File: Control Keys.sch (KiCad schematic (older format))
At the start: 4 parts

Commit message: Fixed PISO Shift Register Wiring
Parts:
- added U?: SN74LVC1G04DBVR, digikey-footprints:SOT-753, symbol dk_Logic-Gates-and-Inverters:SN74LVC1G04DBVR
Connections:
- net GND: now also U?.3 (GND); no longer U?.13 (~SLoad), U?.13 (~SLoad)
- net SHIFT_RCLK: now also U?.2 (A)
- net VCC: now also U?.5 (VCC)
- new net: U?.13 (~SLoad), U?.13 (~SLoad), U?.4 (Y)
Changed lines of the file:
@@
 	4950 1600 4950 2100
-Wire Wire Line
-	4950 1600 6150 1600
 Wire Wire Line
 	6950 1600 6950 2100
@@
 	6250 2300 6400 2300
 Connection ~ 4250 1400
-Wire Wire Line
-	4400 2450 4150 2450
-Wire Wire Line
-	4150 2450 4150 1600
 Connection ~ 4150 1600
 Wire Wire Line
@@
 Connection ~ 4050 1500
 Wire Wire Line
-	6400 2450 6150 2450
-Wire Wire Line
-	6150 2450 6150 1600
-Connection ~ 6150 1600
-Wire Wire Line
-	6150 1600 6800 1600
-Wire Wire Line
 	4050 1500 6050 1500
 Wire Wire Line
@@
 	6050 2550 6050 1500
 Wire Wire Line
-	4150 2450 4150 2750
-Wire Wire Line
 	4150 2750 4400 2750
-Connection ~ 4150 2450
 $Comp
 L Device:C C?
@@
 	9350 1300 9350 3550
 Wire Wire Line
-	1300 1600 1300 4800
+	1300 1600 1300 2000
 Wire Wire Line
 	4650 4800 1300 4800
@@
 	7500 3550 9350 3550
 Wire Wire Line
-	1500 1100 5100 1100
+	1500 1100 2550 1100
 Connection ~ 1500 1100
 Wire Wire Line
@@
 	1000 1400 4250 1400
 Wire Wire Line
-	1000 1500 4050 1500
+	1000 1500 2000 1500
 Wire Wire Line
 	1300 1600 4150 1600
 Connection ~ 1300 1600
-Wire Bus Line
-	4200 2950 4200 4400
-Wire Bus Line
-	6100 2950 6100 4400
-Wire Bus Line
-	6250 4400 6250 6300
 $Sheet
 S 4650 4600 1250 1700
@@
 F3 "GND" I L 2700 5800 50
 $EndSheet
+$Comp
+L dk_Logic-Gates-and-Inverters:SN74LVC1G04DBVR U?
+U 1 1 5EE64350
+P 2000 2100
+AR Path="/5E8C755A/5EE64350" Ref="U?"  Part="1"
+AR Path="/5E8C79BD/5EE64350" Ref="U?"  Part="1"
+F 0 "U?" V 1897 2344 60  0000 L CNN
+F 1 "SN74LVC1G04DBVR" V 2003 2344 60  0000 L CNN
+F 2 "digikey-footprints:SOT-753" H 2200 2300 60  0001 L CNN
+F 3 "http://www.ti.com/general/docs/suppproductinfo.tsp?distId=10&gotoUrl=http%3A%2F%2Fwww.ti.com%2Flit%2Fgpn%2Fsn74lvc1g04" H 2200 2400 60  0001 L CNN
+F 4 "296-11599-1-ND" H 2200 2500 60  0001 L CNN "Digi-Key_PN"
+F 5 "SN74LVC1G04DBVR" H 2200 2600 60  0001 L CNN "MPN"
+F 6 "Integrated Circuits (ICs)" H 2200 2700 60  0001 L CNN "Category"
+F 7 "Logic - Gates and Inverters" H 2200 2800 60  0001 L CNN "Family"
+F 8 "http://www.ti.com/general/docs/suppproductinfo.tsp?distId=10&gotoUrl=http%3A%2F%2Fwww.ti.com%2Flit%2Fgpn%2Fsn74lvc1g04" H 2200 2900 60  0001 L CNN "DK_Datasheet_Link"
+F 9 "/product-detail/en/texas-instruments/SN74LVC1G04DBVR/296-11599-1-ND/385738" H 2200 3000 60  0001 L CNN "DK_Detail_Page"
+F 10 "IC INVERTER 1CH 1-INP SOT23-5" H 2200 3100 60  0001 L CNN "Description"
+F 11 "Texas Instruments" H 2200 3200 60  0001 L CNN "Manufacturer"
+F 12 "Active" H 2200 3300 60  0001 L CNN "Status"
+	1    2000 2100
+	0    1    1    0
+$EndComp
+Wire Wire Line
+	2000 1800 2000 1500
+Connection ~ 2000 1500
+Wire Wire Line
+	2000 1500 4050 1500
+Wire Wire Line
+	1800 2000 1300 2000
+Connection ~ 1300 2000
+Wire Wire Line
+	1300 2000 1300 4800
+Wire Wire Line
+	2200 2100 2550 2100
+Wire Wire Line
+	2550 2100 2550 1100
+Connection ~ 2550 1100
+Wire Wire Line
+	2550 1100 5100 1100
+Wire Wire Line
+	4150 1600 4150 2750
+Wire Wire Line
+	4950 1600 6800 1600
+Wire Wire Line
+	2000 2300 2000 2450
+Wire Wire Line
+	2000 2450 3300 2450
+Wire Wire Line
+	3300 2450 3300 1200
+Wire Wire Line
+	3300 1200 6150 1200
+Wire Wire Line
+	6150 1200 6150 2450
+Wire Wire Line
+	6150 2450 6400 2450
+Wire Bus Line
+	4200 2950 4200 4400
+Wire Bus Line
+	6100 2950 6100 4400
+Wire Bus Line
+	6250 4400 6250 6300
+Connection ~ 3300 2450
+Wire Wire Line
+	3300 2450 4400 2450
 $EndSCHEMATC

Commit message: Corrected errors found in design rule check
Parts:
- removed U? (x2): 74LS597, symbol 74xx_IEEE:74LS597
- added U10, U11: 74LS597, Package_SO:SOIC-16_3.9x9.9mm_P1.27mm, symbol 74xx_IEEE:74LS597
- C43, C44: renamed from C?; footprint (none) -> Capacitor_SMD:C_1206_3216Metric_Pad1.42x1.75mm_HandSolder
- gave numbers to parts that had none: 1
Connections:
- net DEL: now also U10.6 (G)
- net DN: now also U11.3 (D)
- net END: now also U10.7 (H)
- net EXT10: now also U11.7 (H)
- net EXT8: now also U11.5 (F)
- net EXT9: now also U11.6 (G)
- net GND: now also U10.14 (SER), U10.8 (GND), U11.8 (GND)
- net HOME: now also U10.4 (E)
- net INS: now also U10.3 (D)
- net LT: now also U11.2 (C)
- net PAUS: now also U10.2 (C)
- net PGDN: now also U11.15 (A)
- net PGUP: now also U10.5 (F)
- net PRNT: now also U10.15 (A)
- net RESET: now also U10.10 (~R), U11.10 (~R)
- net RT: now also U11.4 (E)
- net SCRL: now also U10.1 (B)
- net SHIFT_4_DATA: now also U11.9 (QH)
- net SHIFT_CLK: now also U10.11 (SCK), U11.11 (SCK)
- net SHIFT_RCLK: now also U10.12 (CLK), U11.12 (CLK)
- net UP: now also U11.1 (B)
- net VCC: now also U10.16 (VCC), U11.16 (VCC)
- net at U9.4 (Y): now also U10.13 (~SLoad), U11.13 (~SLoad)
- new net: U10.9 (QH), U11.14 (SER)
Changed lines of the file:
@@
 Text HLabel 10600 1300 2    50   Output ~ 0
 SHIFT_4_DATA
-$Comp
-L 74xx_IEEE:74LS597 U?
-U 1 1 6064AC4A
-P 4950 2900
-AR Path="/5E8C77AE/6064AC4A" Ref="U?"  Part="1"
-AR Path="/5E8C755A/6064AC4A" Ref="U?"  Part="1"
-AR Path="/5E8C79BD/6064AC4A" Ref="U?"  Part="1"
-F 0 "U?" H 4950 3916 50  0000 C CNN
-F 1 "74LS597" H 4950 3825 50  0000 C CNN
-F 2 "" H 4950 2900 50  0001 C CNN
-F 3 "" H 4950 2900 50  0001 C CNN
-	1    4950 2900
-	1    0    0    -1
-$EndComp
-$Comp
-L 74xx_IEEE:74LS597 U?
-U 1 1 6064AC50
-P 6950 2900
-AR Path="/5E8C77AE/6064AC50" Ref="U?"  Part="1"
-AR Path="/5E8C755A/6064AC50" Ref="U?"  Part="1"
-AR Path="/5E8C79BD/6064AC50" Ref="U?"  Part="1"
-F 0 "U?" H 6950 3916 50  0000 C CNN
-F 1 "74LS597" H 6950 3825 50  0000 C CNN
-F 2 "" H 6950 2900 50  0001 C CNN
-F 3 "" H 6950 2900 50  0001 C CNN
-	1    6950 2900
-	1    0    0    -1
-$EndComp
 Wire Wire Line
 	4250 1400 4250 2300
@@
 Wire Wire Line
 	5600 2750 6400 2750
-Wire Wire Line
-	5100 1100 5100 2100
 Wire Wire Line
 	4950 1600 4950 2100
@@
 Connection ~ 4950 1600
 Wire Wire Line
-	5100 1100 7100 1100
-Wire Wire Line
 	7100 1100 7100 2100
-Connection ~ 5100 1100
 Connection ~ 7100 1100
 Wire Wire Line
@@
 AR Path="/5E8C77AE/6064AC9E" Ref="C?"  Part="1"
 AR Path="/5E8C755A/6064AC9E" Ref="C?"  Part="1"
-AR Path="/5E8C79BD/6064AC9E" Ref="C?"  Part="1"
-F 0 "C?" V 4698 900 50  0000 C CNN
+AR Path="/5E8C79BD/6064AC9E" Ref="C43"  Part="1"
+F 0 "C43" V 4698 900 50  0000 C CNN
 F 1 "1n" V 4789 900 50  0000 C CNN
-F 2 "" H 4988 750 50  0001 C CNN
+F 2 "Capacitor_SMD:C_1206_3216Metric_Pad1.42x1.75mm_HandSolder" H 4988 750 50  0001 C CNN
 F 3 "~" H 4950 900 50  0001 C CNN
 	1    4950 900
@@
 AR Path="/5E8C77AE/6064ACA4" Ref="C?"  Part="1"
 AR Path="/5E8C755A/6064ACA4" Ref="C?"  Part="1"
-AR Path="/5E8C79BD/6064ACA4" Ref="C?"  Part="1"
-F 0 "C?" V 6698 900 50  0000 C CNN
+AR Path="/5E8C79BD/6064ACA4" Ref="C44"  Part="1"
+F 0 "C44" V 6698 900 50  0000 C CNN
 F 1 "1n" V 6789 900 50  0000 C CNN
-F 2 "" H 6988 750 50  0001 C CNN
+F 2 "Capacitor_SMD:C_1206_3216Metric_Pad1.42x1.75mm_HandSolder" H 6988 750 50  0001 C CNN
 F 3 "~" H 6950 900 50  0001 C CNN
 	1    6950 900
 	0    1    1    0
 $EndComp
-Wire Wire Line
-	5100 900  5100 1100
 Wire Wire Line
 	4800 900  4800 1600
@@
 P 2000 2100
 AR Path="/5E8C755A/5EE64350" Ref="U?"  Part="1"
-AR Path="/5E8C79BD/5EE64350" Ref="U?"  Part="1"
-F 0 "U?" V 1897 2344 60  0000 L CNN
+AR Path="/5E8C79BD/5EE64350" Ref="U9"  Part="1"
+F 0 "U9" V 1897 2344 60  0000 L CNN
 F 1 "SN74LVC1G04DBVR" V 2003 2344 60  0000 L CNN
 F 2 "digikey-footprints:SOT-753" H 2200 2300 60  0001 L CNN
@@
 Connection ~ 2550 1100
 Wire Wire Line
+	4150 1600 4150 2750
+Wire Wire Line
+	4950 1600 6800 1600
+Wire Wire Line
+	2000 2300 2000 2450
+Wire Wire Line
+	2000 2450 3300 2450
+Wire Wire Line
+	3300 2450 3300 1200
+Wire Wire Line
+	3300 1200 6150 1200
+Wire Wire Line
+	6150 1200 6150 2450
+Wire Wire Line
+	6150 2450 6400 2450
+Connection ~ 3300 2450
+Wire Wire Line
+	3300 2450 4400 2450
+Wire Wire Line
 	2550 1100 5100 1100
 Wire Wire Line
-	4150 1600 4150 2750
-Wire Wire Line
-	4950 1600 6800 1600
-Wire Wire Line
-	2000 2300 2000 2450
-Wire Wire Line
-	2000 2450 3300 2450
-Wire Wire Line
-	3300 2450 3300 1200
-Wire Wire Line
-	3300 1200 6150 1200
-Wire Wire Line
-	6150 1200 6150 2450
-Wire Wire Line
-	6150 2450 6400 2450
+	5100 2100 5100 1100
+Connection ~ 5100 1100
+Wire Wire Line
+	5100 1100 7100 1100
+Wire Wire Line
+	5100 1100 5100 900
+$Comp
+L 74xx_IEEE:74LS597 U?
+U 1 1 5F0DAE1E
+P 4950 2900
+AR Path="/5E8C77AE/5F0DAE1E" Ref="U?"  Part="1"
+AR Path="/5E8C755A/5F0DAE1E" Ref="U?"  Part="1"
+AR Path="/5E8C79BD/5F0DAE1E" Ref="U10"  Part="1"
+F 0 "U10" H 4950 3916 50  0000 C CNN
+F 1 "74LS597" H 4950 3825 50  0000 C CNN
+F 2 "Package_SO:SOIC-16_3.9x9.9mm_P1.27mm" H 4950 2900 50  0001 C CNN
+F 3 "" H 4950 2900 50  0001 C CNN
+	1    4950 2900
+	1    0    0    -1
+$EndComp
+$Comp
+L 74xx_IEEE:74LS597 U?
+U 1 1 5F0E5779
+P 6950 2900
+AR Path="/5E8C77AE/5F0E5779" Ref="U?"  Part="1"
+AR Path="/5E8C755A/5F0E5779" Ref="U?"  Part="1"
+AR Path="/5E8C79BD/5F0E5779" Ref="U11"  Part="1"
+F 0 "U11" H 6950 3916 50  0000 C CNN
+F 1 "74LS597" H 6950 3825 50  0000 C CNN
+F 2 "Package_SO:SOIC-16_3.9x9.9mm_P1.27mm" H 6950 2900 50  0001 C CNN
+F 3 "" H 6950 2900 50  0001 C CNN
+	1    6950 2900
+	1    0    0    -1
+$EndComp
 Wire Bus Line
 	4200 2950 4200 4400
@@
 Wire Bus Line
 	6250 4400 6250 6300
-Connection ~ 3300 2450
-Wire Wire Line
-	3300 2450 4400 2450
 $EndSCHEMATC

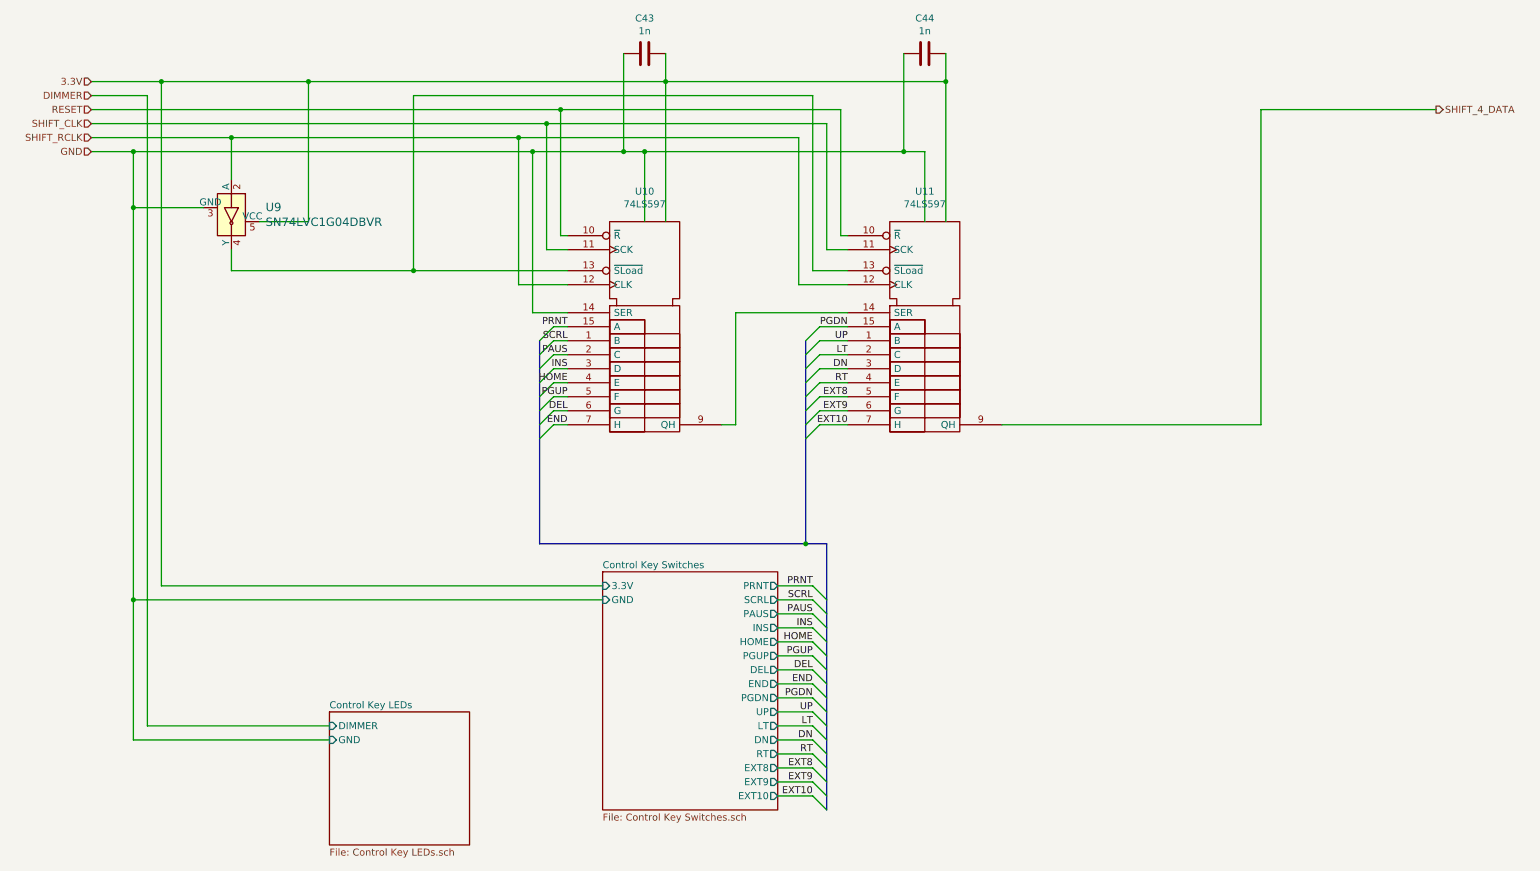
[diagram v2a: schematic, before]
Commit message: Redesigned for single large PCB
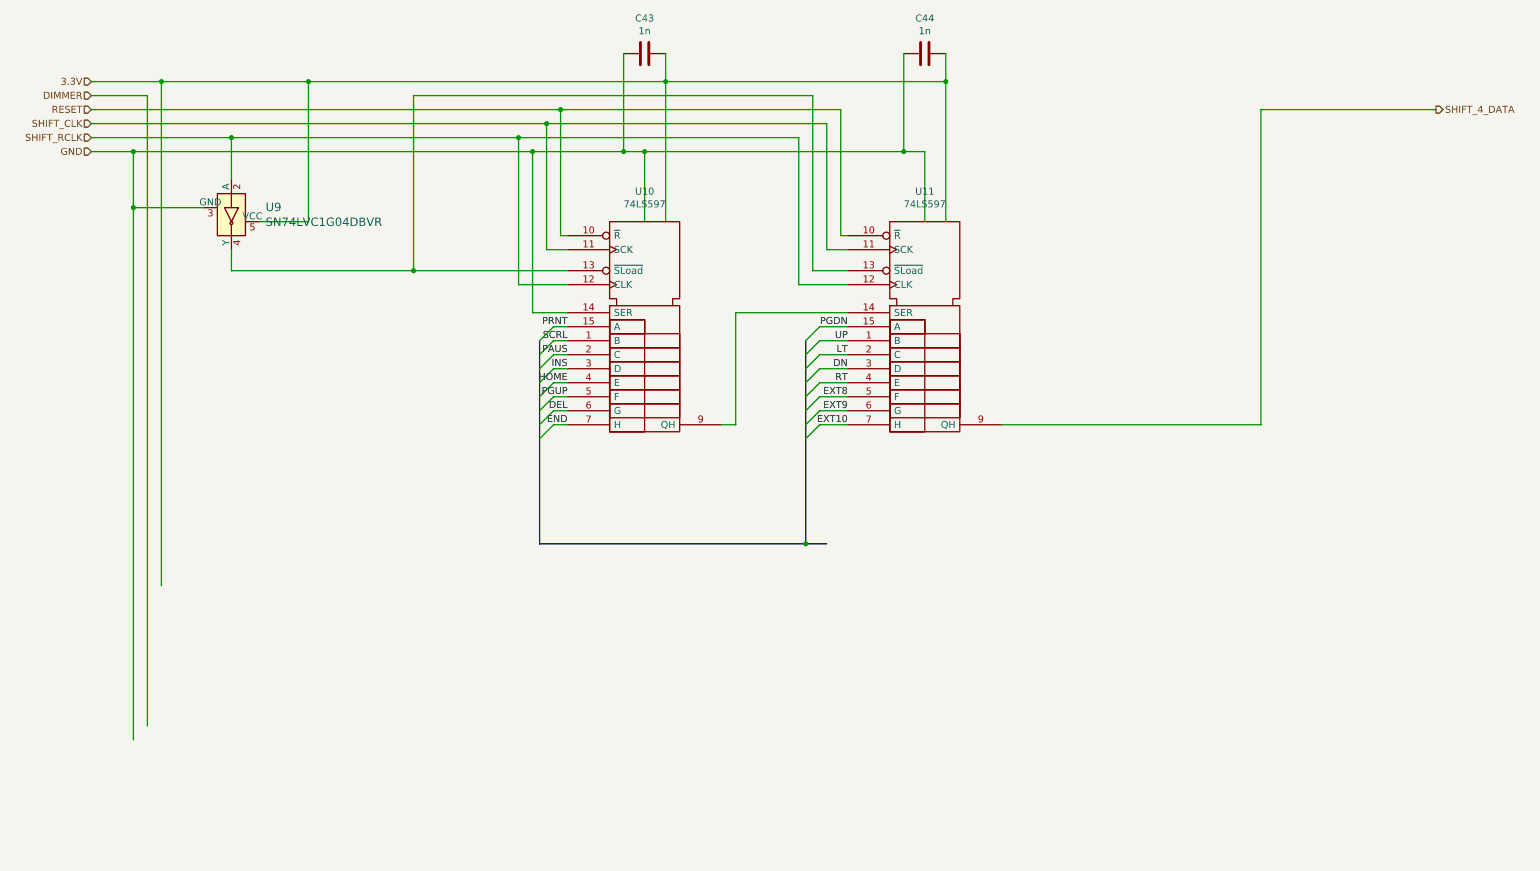
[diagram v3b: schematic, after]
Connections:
- wire segments 98 -> 77
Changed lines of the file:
@@
 $Descr A4 11693 8268
 encoding utf-8
-Sheet 7 18
+Sheet 13 18
 Title ""
 Date ""
@@
 Wire Wire Line
 	9350 1300 10600 1300
-Entry Wire Line
-	6150 4700 6250 4800
-Text Label 6150 4700 2    50   ~ 0
-PRNT
-Text Label 6150 4800 2    50   ~ 0
-SCRL
-Text Label 6150 4900 2    50   ~ 0
-PAUS
-Text Label 6150 5000 2    50   ~ 0
-INS
-Text Label 6150 5100 2    50   ~ 0
-HOME
-Text Label 6150 5200 2    50   ~ 0
-PGUP
-Text Label 6150 5300 2    50   ~ 0
-DEL
-Text Label 6150 5400 2    50   ~ 0
-END
-Text Label 6150 5500 2    50   ~ 0
-PGDN
-Text Label 6150 5600 2    50   ~ 0
-UP
-Text Label 6150 5700 2    50   ~ 0
-LT
-Text Label 6150 5800 2    50   ~ 0
-DN
-Text Label 6150 5900 2    50   ~ 0
-RT
-Text Label 6150 6000 2    50   ~ 0
-EXT8
-Text Label 6150 6100 2    50   ~ 0
-EXT9
-Text Label 6150 6200 2    50   ~ 0
-EXT10
-Entry Wire Line
-	6150 4800 6250 4900
-Entry Wire Line
-	6150 4900 6250 5000
-Entry Wire Line
-	6150 5000 6250 5100
-Entry Wire Line
-	6150 5100 6250 5200
-Entry Wire Line
-	6150 5200 6250 5300
-Entry Wire Line
-	6150 5300 6250 5400
-Entry Wire Line
-	6150 5400 6250 5500
 Wire Wire Line
 	4400 2850 4300 2850
@@
 EXT10
 Entry Wire Line
-	6150 5500 6250 5600
-Entry Wire Line
-	6150 5600 6250 5700
-Entry Wire Line
-	6150 5700 6250 5800
-Entry Wire Line
-	6150 5800 6250 5900
-Entry Wire Line
-	6150 5900 6250 6000
-Entry Wire Line
-	6150 6000 6250 6100
-Entry Wire Line
-	6150 6100 6250 6200
-Entry Wire Line
-	6150 6200 6250 6300
-Entry Wire Line
 	4200 2950 4300 2850
 Entry Wire Line
@@
 	1400 1200 1400 5700
 Wire Wire Line
-	1400 5700 2700 5700
-Wire Wire Line
 	1500 1100 1500 4700
 Wire Wire Line
-	1300 5800 2700 5800
-Wire Wire Line
 	9350 1300 9350 3550
 Wire Wire Line
 	1300 1600 1300 2000
-Wire Wire Line
-	4650 4800 1300 4800
-Connection ~ 1300 4800
-Wire Wire Line
-	1300 4800 1300 5800
-Wire Wire Line
-	5900 4700 6150 4700
-Wire Wire Line
-	5900 4800 6150 4800
-Wire Wire Line
-	5900 4900 6150 4900
-Wire Wire Line
-	5900 5000 6150 5000
-Wire Wire Line
-	5900 5100 6150 5100
-Wire Wire Line
-	5900 5200 6150 5200
-Wire Wire Line
-	5900 5300 6150 5300
-Wire Wire Line
-	5900 5400 6150 5400
-Wire Wire Line
-	5900 5500 6150 5500
-Wire Wire Line
-	5900 5600 6150 5600
-Wire Wire Line
-	5900 5700 6150 5700
-Wire Wire Line
-	5900 5800 6150 5800
-Wire Wire Line
-	5900 5900 6150 5900
-Wire Wire Line
-	5900 6000 6150 6000
-Wire Wire Line
-	5900 6100 6150 6100
-Wire Wire Line
-	5900 6200 6150 6200
-Wire Wire Line
-	1500 4700 4650 4700
 Wire Wire Line
 	6200 2850 6400 2850
@@
 	1300 1600 4150 1600
 Connection ~ 1300 1600
-$Sheet
-S 4650 4600 1250 1700
-U 606B9FCC
-F0 "Control Key Switches" 50
-F1 "Control Key Switches.sch" 50
-F2 "3.3V" I L 4650 4700 50
-F3 "GND" I L 4650 4800 50
-F4 "PRNT" O R 5900 4700 50
-F5 "SCRL" O R 5900 4800 50
-F6 "PAUS" O R 5900 4900 50
-F7 "INS" O R 5900 5000 50
-F8 "HOME" O R 5900 5100 50
-F9 "PGUP" O R 5900 5200 50
-F10 "DEL" O R 5900 5300 50
-F11 "END" O R 5900 5400 50
-F12 "PGDN" O R 5900 5500 50
-F13 "EXT8" O R 5900 6000 50
-F14 "EXT9" O R 5900 6100 50
-F15 "EXT10" O R 5900 6200 50
-F16 "UP" O R 5900 5600 50
-F17 "LT" O R 5900 5700 50
-F18 "DN" O R 5900 5800 50
-F19 "RT" O R 5900 5900 50
-$EndSheet
-$Sheet
-S 2700 5600 1000 950
-U 60A725E0
-F0 "Control Key LEDs" 50
-F1 "Control Key LEDs.sch" 50
-F2 "DIMMER" I L 2700 5700 50
-F3 "GND" I L 2700 5800 50
-$EndSheet
 $Comp
 L dk_Logic-Gates-and-Inverters:SN74LVC1G04DBVR U?
@@
 Connection ~ 1300 2000
 Wire Wire Line
-	1300 2000 1300 4800
-Wire Wire Line
 	2200 2100 2550 2100
 Wire Wire Line
@@
 	1    0    0    -1
 $EndComp
+Wire Wire Line
+	1300 2000 1300 5800
 Wire Bus Line
 	4200 2950 4200 4400
 Wire Bus Line
 	6100 2950 6100 4400
-Wire Bus Line
-	6250 4400 6250 6300
 $EndSCHEMATC
